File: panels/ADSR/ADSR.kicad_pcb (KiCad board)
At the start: 2 copper layers, 70.8 x 128.4 mm, 12 parts

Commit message: sequencer work
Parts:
- added REF**: Jack_3.5mm, FormantKO-Panel:Jack_3.5mm, F.Cu at (84.6, 138.7)
- moved REF** 17.0 mm to (101.6, 139.3)
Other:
- board text added: "GATE"

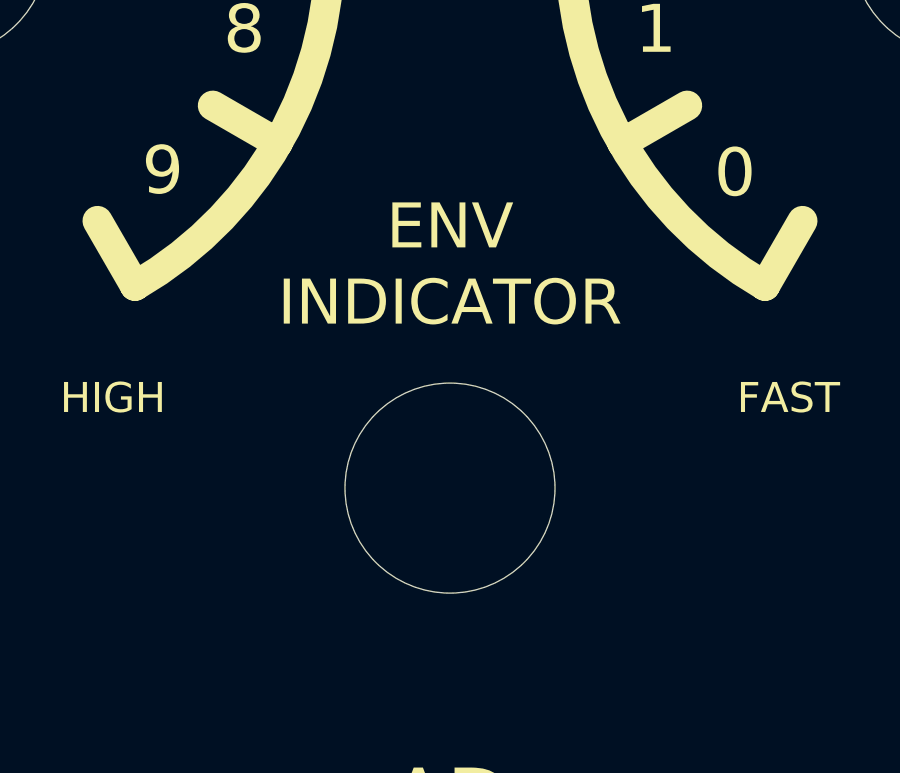
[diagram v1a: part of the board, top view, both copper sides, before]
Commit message: updated ADSR panel to add gate input and change led
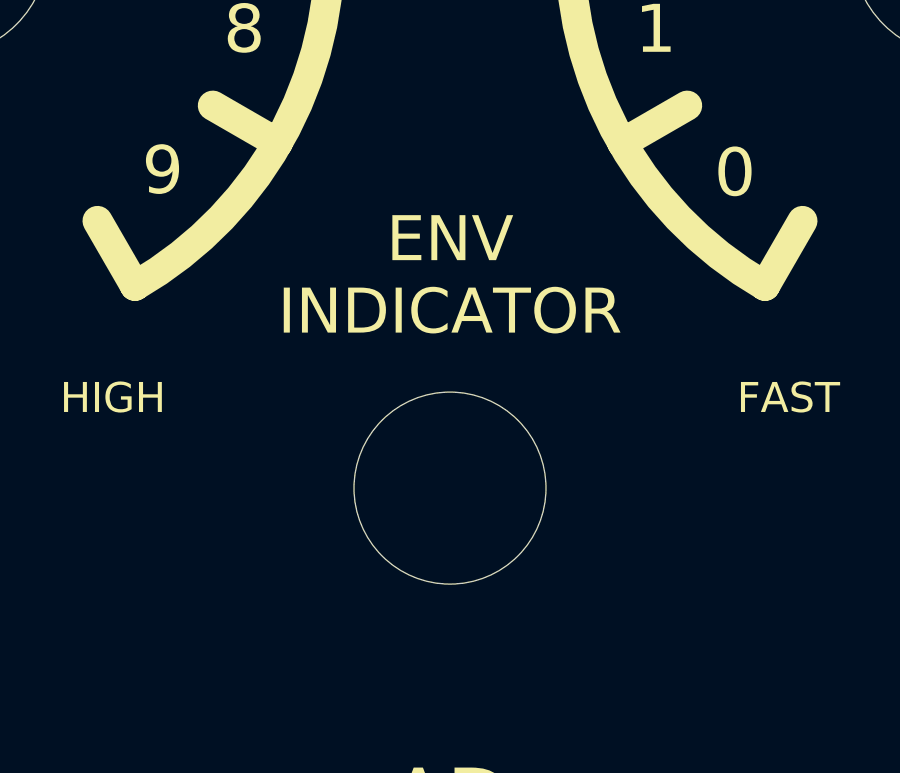
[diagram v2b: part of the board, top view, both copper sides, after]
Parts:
- removed the REF** at (101.6, 121.7)
- added REF**: LED_3mm_6mm_Bezel, FormantKO-Panel:LED_3mm_6mm_Bezel, F.Cu at (101.6, 121.7)
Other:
- board text added: "ENV INDICATOR"
- board text removed: "ENV"
- board text removed: "INDICATOR"
